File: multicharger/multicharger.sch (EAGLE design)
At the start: 25 parts, among them J2 USB-MICROA-AMPHENOL-10118192-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, J3 HEADER-8POS-, P1 TEST-POINT, P2 TEST-POINT, P3 TEST-POINT, P4 TEST-POINT, P5 TEST-POINT, P6 TEST-POINT, U1 MCP73831T-2ACI/OT, U2 MCP73831T-2ACI/OT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

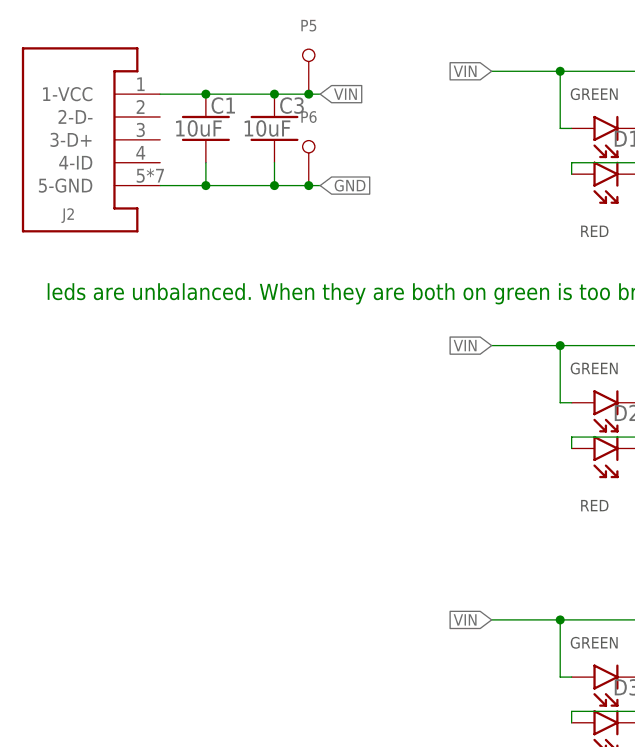
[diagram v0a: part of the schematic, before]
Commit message: pretty, compact, USB-A version of multicharger
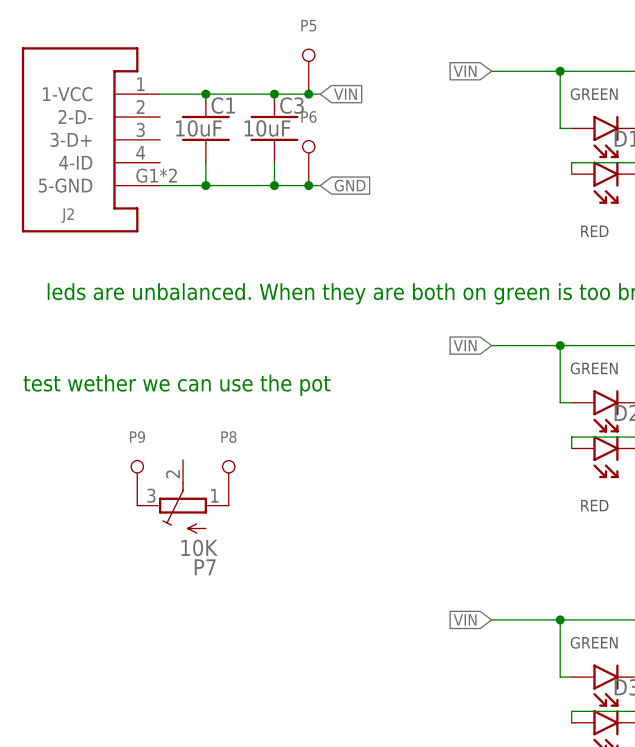
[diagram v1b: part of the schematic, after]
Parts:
- added P7: 10K, RemoteParts:TRIMPOT-BOT-ADJUST
- added P8, P9: TEST-POINT-1MM, RemoteParts:TEST-POINT-1MM
- J2: value USB-MICROA-AMPHENOL-10118192-0001LF -> USB-A-SMD-KEYSTONE-931; device RemoteParts:USB-MICROA-AMPHENOL-10118192-0001LF -> RemoteParts:USB-A-SMD-KEYSTONE-931
- P1, P2, P3, P4, P5, P6: value TEST-POINT -> TEST-POINT-1MM; device RemoteParts:TEST-POINT -> RemoteParts:TEST-POINT-1MM
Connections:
- new net N$17: P7.A, P8.T
- new net N$18: P7.E, P9.T
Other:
- note added: "test wether we can use the pot"
- moved on the sheet: J2
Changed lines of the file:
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@@
 <setting verticaltext="up"/>
 </settings>
-<grid distance="0.1" unitdist="inch" unit="inch" style="lines" multiple="1" display="no" altdistance="0.01" altunitdist="inch" altunit="inch"/>
+<grid distance="0.05" unitdist="inch" unit="inch" style="lines" multiple="1" display="no" altdistance="0.01" altunitdist="inch" altunit="inch"/>
 <layers>
 <layer number="1" name="Top" color="4" fill="1" visible="no" active="no"/>
@@
 <part name="R5" library="quadparts_prebuilt" deviceset="RESISTOR-PACK-4X" device="-2K" package3d_urn="urn:adsk.eagle:package:10895048/1" value="2K"/>
 <part name="FRAME1" library="quadparts_prebuilt" deviceset="FRAME_B_L" device=""/>
-<part name="J2" library="RemoteParts" deviceset="USB" device="-MICROA-AMPHENOL-10118192-0001LF"/>
+<part name="J2" library="RemoteParts" deviceset="USB" device="-A-SMD-KEYSTONE-931" value="USB-A-SMD-KEYSTONE-931"/>
 <part name="J3" library="quadparts_prebuilt" deviceset="HEADER-8POS-" device="">
 <attribute name="PIN1" value="-"/>
@@
 <attribute name="PIN8" value="+"/>
 </part>
-<part name="P1" library="RemoteParts" deviceset="TEST-POINT" device=""/>
-<part name="P2" library="RemoteParts" deviceset="TEST-POINT" device=""/>
-<part name="P3" library="RemoteParts" deviceset="TEST-POINT" device=""/>
-<part name="P4" library="RemoteParts" deviceset="TEST-POINT" device=""/>
-<part name="P5" library="RemoteParts" deviceset="TEST-POINT" device=""/>
-<part name="P6" library="RemoteParts" deviceset="TEST-POINT" device=""/>
+<part name="P1" library="RemoteParts" deviceset="TEST-POINT" device="-1MM" value="TEST-POINT-1MM"/>
+<part name="P2" library="RemoteParts" deviceset="TEST-POINT" device="-1MM" value="TEST-POINT-1MM"/>
+<part name="P3" library="RemoteParts" deviceset="TEST-POINT" device="-1MM" value="TEST-POINT-1MM"/>
+<part name="P4" library="RemoteParts" deviceset="TEST-POINT" device="-1MM" value="TEST-POINT-1MM"/>
+<part name="P5" library="RemoteParts" deviceset="TEST-POINT" device="-1MM" value="TEST-POINT-1MM"/>
+<part name="P6" library="RemoteParts" deviceset="TEST-POINT" device="-1MM" value="TEST-POINT-1MM"/>
 <part name="C1" library="quadparts_prebuilt" deviceset="CAPACITOR-NP_" device="SMD-0603_CERAMIC-10UF" package3d_urn="urn:adsk.eagle:package:11135716/1" value="10uF"/>
 <part name="C3" library="quadparts_prebuilt" deviceset="CAPACITOR-NP_" device="SMD-0603_CERAMIC-10UF" package3d_urn="urn:adsk.eagle:package:11135716/1" value="10uF"/>
+<part name="P7" library="RemoteParts" deviceset="TRIMPOT" device="-BOT-ADJUST" value="10K"/>
+<part name="P8" library="RemoteParts" deviceset="TEST-POINT" device="-1MM" value="TEST-POINT-1MM"/>
+<part name="P9" library="RemoteParts" deviceset="TEST-POINT" device="-1MM" value="TEST-POINT-1MM"/>
 </parts>
 <sheets>
@@
 2.2KOhm -&gt; 450mA</text>
 <text x="99.06" y="162.56" size="1.778" layer="91">leds are unbalanced. When they are both on green is too bright.</text>
+<text x="96.52" y="152.4" size="1.778" layer="91">test wether we can use the pot</text>
 </plain>
 <instances>
@@
 <attribute name="VALUE" x="120.904" y="180.721" size="1.778" layer="96"/>
 <attribute name="NAME" x="124.968" y="183.261" size="1.778" layer="95"/>
+</instance>
+<instance part="P7" gate="G$1" x="114.3" y="139.7" smashed="yes" rot="R90">
+<attribute name="VALUE" x="118.11" y="135.89" size="1.778" layer="96" rot="R180"/>
+<attribute name="NAME" x="118.11" y="133.731" size="1.778" layer="95" rot="R180"/>
+</instance>
+<instance part="P8" gate="G$1" x="119.38" y="139.7" smashed="yes">
+<attribute name="NAME" x="119.38" y="147.32" size="1.27" layer="95" align="center"/>
+</instance>
+<instance part="P9" gate="G$1" x="109.22" y="139.7" smashed="yes">
+<attribute name="NAME" x="109.22" y="147.32" size="1.27" layer="95" align="center"/>
 </instance>
 </instances>
@@
 </segment>
 </net>
+<net name="N$17" class="0">
+<segment>
+<pinref part="P7" gate="G$1" pin="A"/>
+<pinref part="P8" gate="G$1" pin="T"/>
+</segment>
+</net>
+<net name="N$18" class="0">
+<segment>
+<pinref part="P7" gate="G$1" pin="E"/>
+<pinref part="P9" gate="G$1" pin="T"/>
+</segment>
+</net>
